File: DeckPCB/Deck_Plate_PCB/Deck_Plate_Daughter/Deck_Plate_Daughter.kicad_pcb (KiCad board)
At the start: 2 copper layers, 36 parts, among them J1 SunnyBuddy_Inhibit, J2 JST_Batt_Conn, J3 Motor_Inhibit, J4 BurnWire_Inhibit, J5 Power, J6 Raspberry_Pi_2_3, J7 Board_to_Board, Q1 Device_Q_NPN_BCE, U2 SunnyBuddy_Breakout, U3 Big_Easy_Driver, U4 TTL_Camera, U5 Adafruit_INA219_Breakout

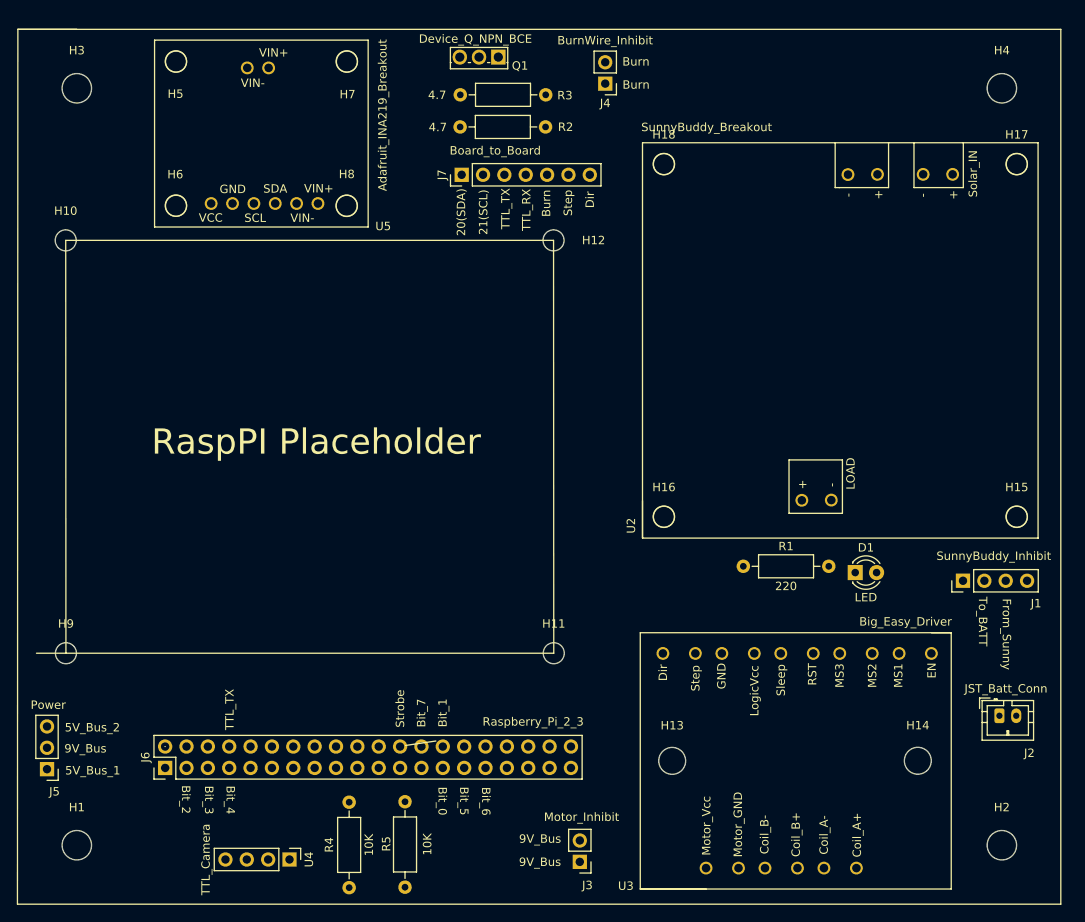
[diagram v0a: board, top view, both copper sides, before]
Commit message: Started routing of Deck_Plate_PCB, the main board.
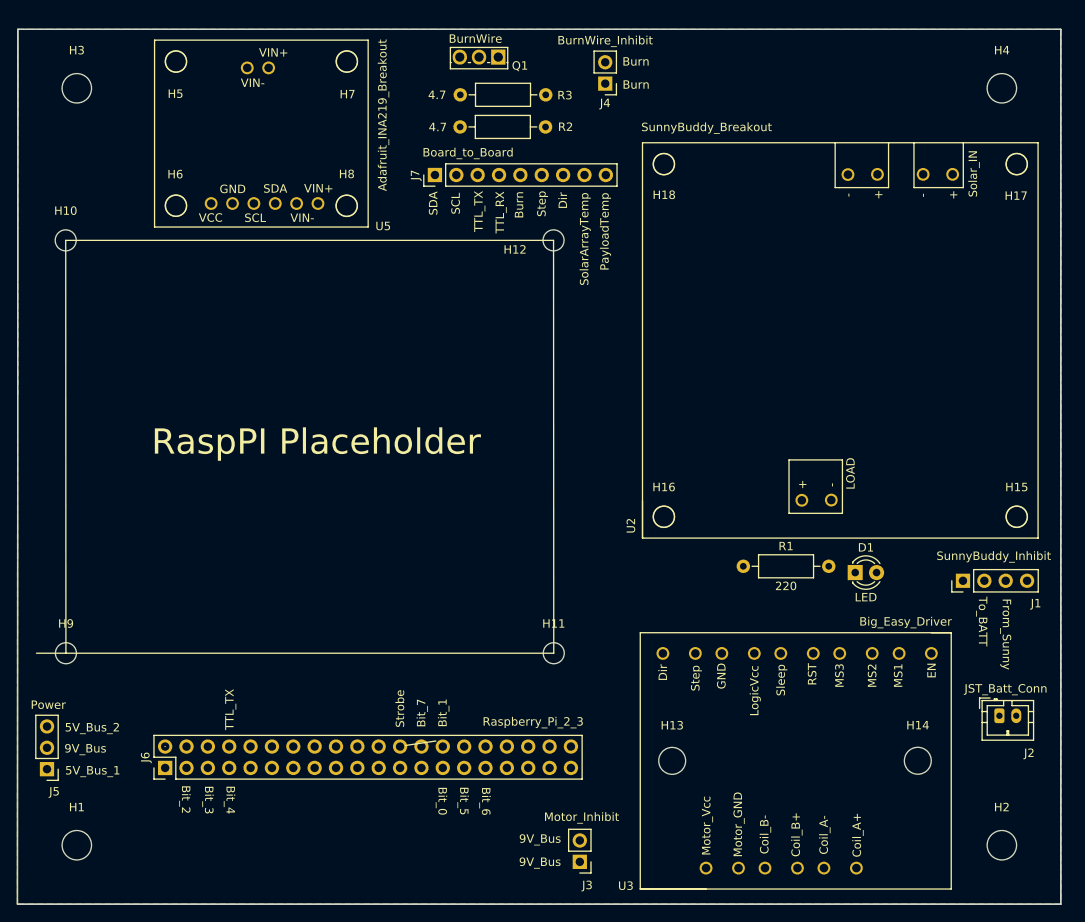
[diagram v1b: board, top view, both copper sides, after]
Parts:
- removed R4, R5: 10K, Resistor_THT:R_Axial_DIN0207_L6.3mm_D2.5mm_P10.16mm_Horizontal
- removed U4: TTL_Camera, Connector_PinHeader_2.54mm:PinHeader_1x04_P2.54mm_Vertical
- J7: footprint Connector_PinHeader_2.54mm:PinHeader_1x07_P2.54mm_Vertical -> Connector_PinHeader_2.54mm:PinHeader_1x09_P2.54mm_Vertical
- Q1: value Device_Q_NPN_BCE -> BurnWire
- moved J7 3.18 mm to (128.5, 60.8)
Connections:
- net /20(SDA) renamed /SDA
- net /21(SCL) renamed /SCL
- J6 pad 8: /TTL_TX -> Net-(J6-Pad8)
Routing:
- added copper zone on B.Cu, net GND
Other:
- board outline added: 124.1 x 104 mm
- board text added: "PayloadTemp"
- board text added: "SCL"
- board text added: "SDA"
- board text added: "SolarArrayTemp"
- board text removed: "20(SDA)"
- board text removed: "21(SCL)"

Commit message: Finised routing fro Main_Board, Daughter_Board, and BurnWire circuits. Creating SensorEndPanel board next.
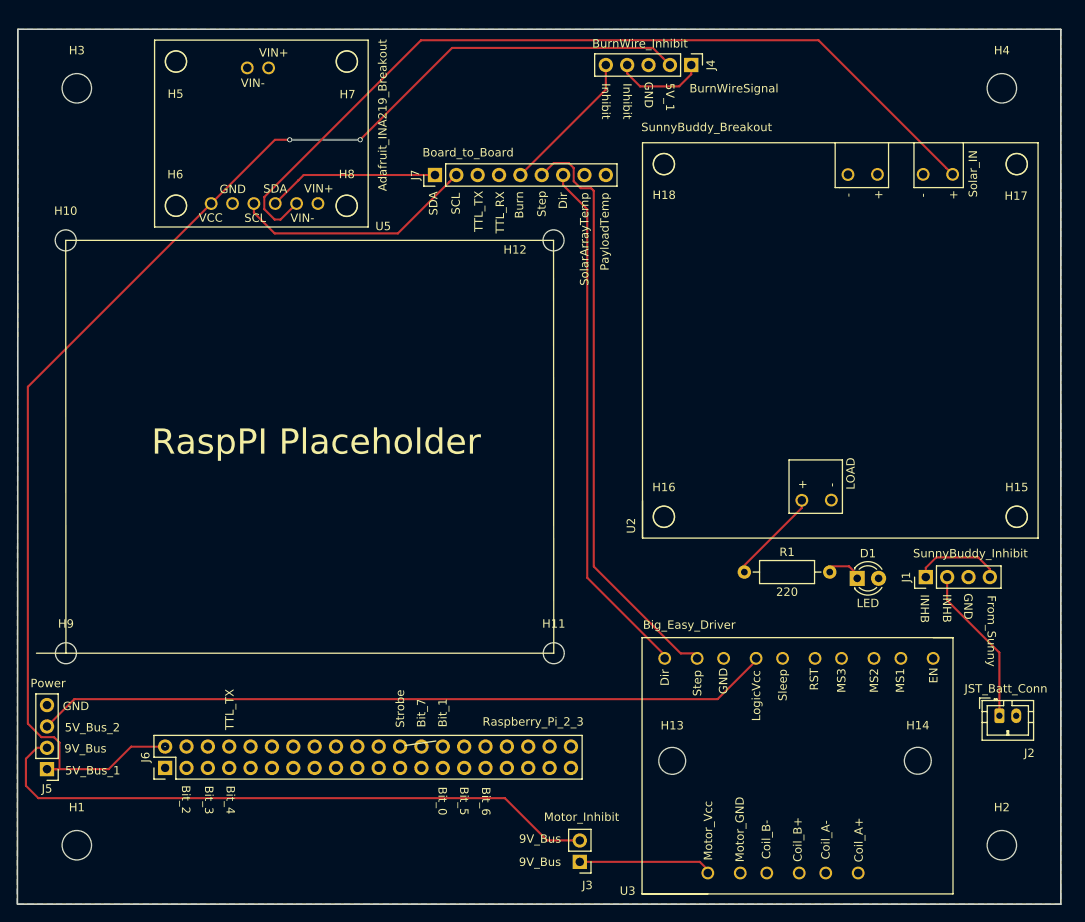
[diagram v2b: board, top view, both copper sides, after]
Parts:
- removed Q1: BurnWire, Package_TO_SOT_THT:TO-251-3_Vertical
- removed R2, R3: 4.7, Resistor_THT:R_Axial_DIN0207_L6.3mm_D2.5mm_P10.16mm_Horizontal
- J4: footprint Connector_PinHeader_2.54mm:PinHeader_1x02_P2.54mm_Vertical -> Connector_PinHeader_2.54mm:PinHeader_1x05_P2.54mm_Vertical
- J5: footprint Connector_PinHeader_2.54mm:PinHeader_1x03_P2.54mm_Vertical -> Connector_PinHeader_2.54mm:PinHeader_1x04_P2.54mm_Vertical
- moved J4 10.5 mm to (159.0, 47.8), turned to 270 degrees
- moved J1 4.45 mm to (186.9, 108.6)
- moved D1 0.73 mm to (178.7, 108.8)
- moved R1 0.70 mm to (165.3, 108.1)
- moved U3 0.62 mm to (190.1, 115.8)
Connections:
- J1 pad 1: GND -> /Sunny_Batt_Out
- J1 pad 3: /Sunny_Batt_Out -> GND
- J1 pad 4: GND -> /Sunny_Batt_Out
- J4 pad 2: /BurnWireSignal -> /5V_Bus_1
- U2 pad 1: /Solar_IN- -> GND
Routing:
- net /5V_Bus_1: track 0.00 -> 158.4 mm, vias 0 -> 2
- net /Solar_IN+: track 0.00 -> 102.8 mm
- net /9V_Bus: track 0.00 -> 90.1 mm
- net /5V_Bus_2: track 0.00 -> 88.3 mm
- net /Step: track 0.00 -> 70.1 mm
- net /Dir: track 0.00 -> 61.8 mm
- net /SCL: track 0.00 -> 29.1 mm
- net /BurnWireSignal: track 0.00 -> 28.3 mm
- net /SDA: track 0.00 -> 20.4 mm
- net /Batt_IN: track 0.00 -> 19.1 mm
- net /Sunny_Batt_Out: track 0.00 -> 10.8 mm
- net Net-(R1-Pad1): track 0.00 -> 10.7 mm
- net Net-(D1-Pad1): track 0.00 -> 3.45 mm
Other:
- board text added: "5V_1"
- board text added: "BurnWireSignal"
- board text added: "GND"
- board text added: "INHB"
- board text added: "Inhibit"
- board text removed: "To_BATT"

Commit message: updated PCB routing and creation of BurnWire circuit board and updated Daughter_Board
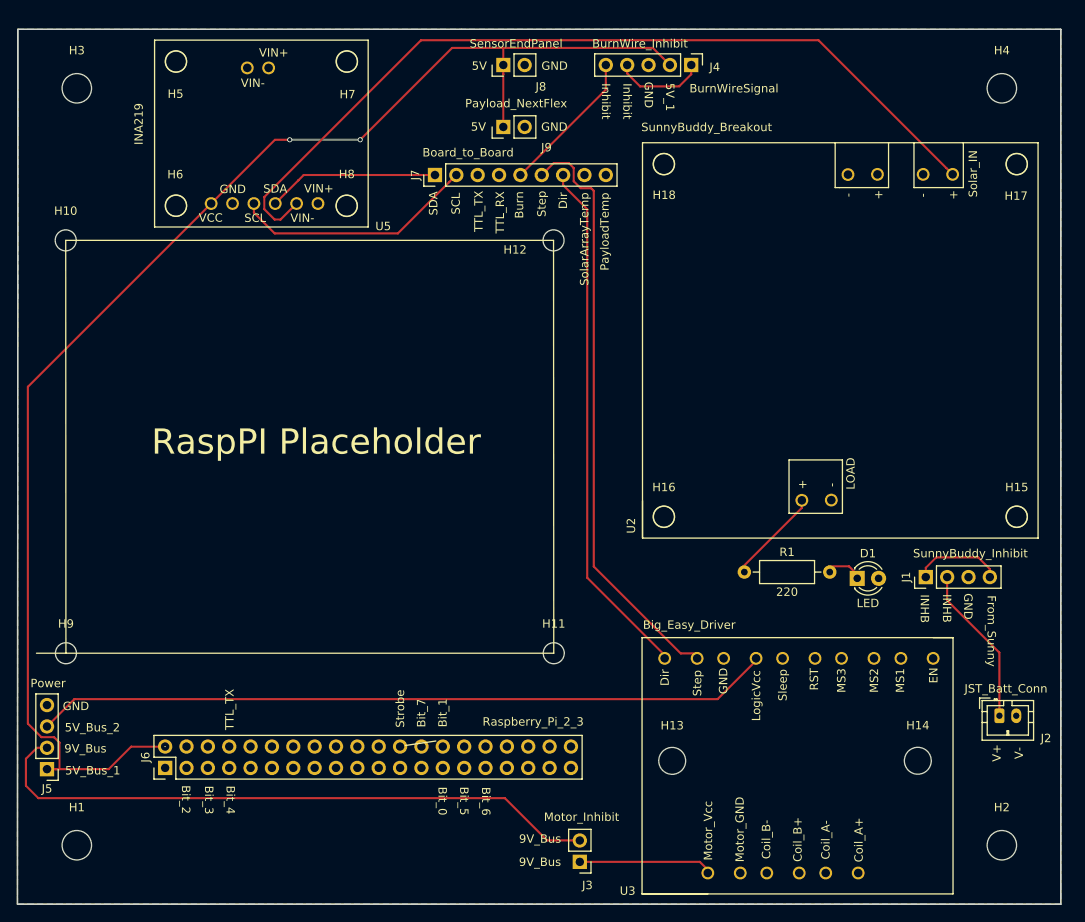
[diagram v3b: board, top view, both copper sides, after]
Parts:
- added J8: SensorEndPanel, Connector_PinHeader_2.54mm:PinHeader_1x02_P2.54mm_Vertical, F.Cu at (136.7, 47.8)
- added J9: Payload_NextFlex, Connector_PinHeader_2.54mm:PinHeader_1x02_P2.54mm_Vertical, F.Cu at (136.7, 55.1)
- U5: value Adafruit_INA219_Breakout -> INA219
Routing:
- net /5V_Bus_1: track 158.4 -> 167.8 mm
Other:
- board text added: "5V"
- board text added: "V+"
- board text added: "V-"
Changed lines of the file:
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@@
   (general
     (thickness 1.6)
-    (drawings 51)
-    (tracks 86)
+    (drawings 57)
+    (tracks 90)
     (zones 0)
-    (modules 30)
+    (modules 32)
     (nets 61)
   )
@@
     (add_net "Net-(U3-Pad6)")
   )
+  (module Connector_PinHeader_2.54mm:PinHeader_1x02_P2.54mm_Vertical (layer F.Cu)
+    (at 136.652 55.118 90)
+    (descr "Through hole straight pin header, 1x02, 2.54mm pitch, single row")
+    (tags "Through hole pin header THT 1x02 2.54mm single row")
+    (fp_text reference J9 (at -2.442 5.128 180) (layer F.SilkS)
+      (effects (font (size 1 1) (thickness 0.15)))
+    )
+    (fp_text value Payload_NextFlex (at 2.794 1.524 180) (layer F.SilkS)
+      (effects (font (size 1 1) (thickness 0.15)))
+    )
+    (fp_text user %R (at 0 1.27) (layer F.Fab)
+      (effects (font (size 1 1) (thickness 0.15)))
+    )
+    (fp_line (start 1.8 -1.8) (end -1.8 -1.8) (layer F.CrtYd) (width 0.05))
+    (fp_line (start 1.8 4.35) (end 1.8 -1.8) (layer F.CrtYd) (width 0.05))
+    (fp_line (start -1.8 4.35) (end 1.8 4.35) (layer F.CrtYd) (width 0.05))
+    (fp_line (start -1.8 -1.8) (end -1.8 4.35) (layer F.CrtYd) (width 0.05))
+    (fp_line (start -1.33 -1.33) (end 0 -1.33) (layer F.SilkS) (width 0.12))
+    (fp_line (start -1.33 0) (end -1.33 -1.33) (layer F.SilkS) (width 0.12))
+    (fp_line (start -1.33 1.27) (end 1.33 1.27) (layer F.SilkS) (width 0.12))
+    (fp_line (start 1.33 1.27) (end 1.33 3.87) (layer F.SilkS) (width 0.12))
+    (fp_line (start -1.33 1.27) (end -1.33 3.87) (layer F.SilkS) (width 0.12))
+    (fp_line (start -1.33 3.87) (end 1.33 3.87) (layer F.SilkS) (width 0.12))
+    (fp_line (start -1.27 -0.635) (end -0.635 -1.27) (layer F.Fab) (width 0.1))
+    (fp_line (start -1.27 3.81) (end -1.27 -0.635) (layer F.Fab) (width 0.1))
+    (fp_line (start 1.27 3.81) (end -1.27 3.81) (layer F.Fab) (width 0.1))
+    (fp_line (start 1.27 -1.27) (end 1.27 3.81) (layer F.Fab) (width 0.1))
+    (fp_line (start -0.635 -1.27) (end 1.27 -1.27) (layer F.Fab) (width 0.1))
+    (pad 2 thru_hole oval (at 0 2.54 90) (size 1.7 1.7) (drill 1) (layers *.Cu *.Mask)
+      (net 1 GND))
+    (pad 1 thru_hole rect (at 0 0 90) (size 1.7 1.7) (drill 1) (layers *.Cu *.Mask)
+      (net 7 /5V_Bus_1))
+    (model ${KISYS3DMOD}/Connector_PinHeader_2.54mm.3dshapes/PinHeader_1x02_P2.54mm_Vertical.wrl
+      (at (xyz 0 0 0))
+      (scale (xyz 1 1 1))
+      (rotate (xyz 0 0 0))
+    )
+  )
+  (module Connector_PinHeader_2.54mm:PinHeader_1x02_P2.54mm_Vertical (layer F.Cu)
+    (at 136.652 47.752 90)
+    (descr "Through hole straight pin header, 1x02, 2.54mm pitch, single row")
+    (tags "Through hole pin header THT 1x02 2.54mm single row")
+    (fp_text reference J8 (at -2.578 4.468 180) (layer F.SilkS)
+      (effects (font (size 1 1) (thickness 0.15)))
+    )
+    (fp_text value SensorEndPanel (at 2.54 1.524 180) (layer F.SilkS)
+      (effects (font (size 1 1) (thickness 0.15)))
+    )
+    (fp_text user %R (at 0 1.27) (layer F.Fab)
+      (effects (font (size 1 1) (thickness 0.15)))
+    )
+    (fp_line (start 1.8 -1.8) (end -1.8 -1.8) (layer F.CrtYd) (width 0.05))
+    (fp_line (start 1.8 4.35) (end 1.8 -1.8) (layer F.CrtYd) (width 0.05))
+    (fp_line (start -1.8 4.35) (end 1.8 4.35) (layer F.CrtYd) (width 0.05))
+    (fp_line (start -1.8 -1.8) (end -1.8 4.35) (layer F.CrtYd) (width 0.05))
+    (fp_line (start -1.33 -1.33) (end 0 -1.33) (layer F.SilkS) (width 0.12))
+    (fp_line (start -1.33 0) (end -1.33 -1.33) (layer F.SilkS) (width 0.12))
+    (fp_line (start -1.33 1.27) (end 1.33 1.27) (layer F.SilkS) (width 0.12))
+    (fp_line (start 1.33 1.27) (end 1.33 3.87) (layer F.SilkS) (width 0.12))
+    (fp_line (start -1.33 1.27) (end -1.33 3.87) (layer F.SilkS) (width 0.12))
+    (fp_line (start -1.33 3.87) (end 1.33 3.87) (layer F.SilkS) (width 0.12))
+    (fp_line (start -1.27 -0.635) (end -0.635 -1.27) (layer F.Fab) (width 0.1))
+    (fp_line (start -1.27 3.81) (end -1.27 -0.635) (layer F.Fab) (width 0.1))
+    (fp_line (start 1.27 3.81) (end -1.27 3.81) (layer F.Fab) (width 0.1))
+    (fp_line (start 1.27 -1.27) (end 1.27 3.81) (layer F.Fab) (width 0.1))
+    (fp_line (start -0.635 -1.27) (end 1.27 -1.27) (layer F.Fab) (width 0.1))
+    (pad 2 thru_hole oval (at 0 2.54 90) (size 1.7 1.7) (drill 1) (layers *.Cu *.Mask)
+      (net 1 GND))
+    (pad 1 thru_hole rect (at 0 0 90) (size 1.7 1.7) (drill 1) (layers *.Cu *.Mask)
+      (net 7 /5V_Bus_1))
+    (model ${KISYS3DMOD}/Connector_PinHeader_2.54mm.3dshapes/PinHeader_1x02_P2.54mm_Vertical.wrl
+      (at (xyz 0 0 0))
+      (scale (xyz 1 1 1))
+      (rotate (xyz 0 0 0))
+    )
+  )
   (module Connector_PinHeader_2.54mm:PinHeader_1x05_P2.54mm_Vertical (layer F.Cu)
     (at 159.004 47.752 270)
     (descr "Through hole straight pin header, 1x05, 2.54mm pitch, single row")
     (tags "Through hole pin header THT 1x05 2.54mm single row")
-    (fp_text reference J4 (at 0 -2.33 90) (layer F.SilkS)
+    (fp_text reference J4 (at 0.254 -2.794 180) (layer F.SilkS)
       (effects (font (size 1 1) (thickness 0.15)))
     )
@@
       (effects (font (size 1 1) (thickness 0.15)))
     )
-    (fp_text value Adafruit_INA219_Breakout (at 27.1272 8.9281 90) (layer F.SilkS)
+    (fp_text value INA219 (at -1.86888 9.9771 90) (layer F.SilkS)
       (effects (font (size 1 1) (thickness 0.15)))
     )
@@
     (descr "JST PH series connector, B2B-PH-K (http://www.jst-mfg.com/product/pdf/eng/ePH.pdf), generated with kicad-footprint-generator")
     (tags "connector JST PH side entry")
-    (fp_text reference J2 (at 3.56108 4.43992) (layer F.SilkS)
+    (fp_text reference J2 (at 5.53888 2.67928) (layer F.SilkS)
       (effects (font (size 1 1) (thickness 0.15)))
     )
@@
       (rotate (xyz 0 0 0))
     )
+  )
+  (gr_text V- (at 197.99 129.58 90) (layer F.SilkS)
+    (effects (font (size 1 1) (thickness 0.15)))
+  )
+  (gr_text V+ (at 195.34 129.57 90) (layer F.SilkS)
+    (effects (font (size 1 1) (thickness 0.15)))
+  )
+  (gr_text 5V (at 133.8 47.86) (layer F.SilkS)
+    (effects (font (size 1 1) (thickness 0.15)))
+  )
+  (gr_text GND (at 142.75 47.86) (layer F.SilkS)
+    (effects (font (size 1 1) (thickness 0.15)))
+  )
+  (gr_text GND (at 142.72 55.11) (layer F.SilkS)
+    (effects (font (size 1 1) (thickness 0.15)))
+  )
+  (gr_text 5V (at 133.7 55.1) (layer F.SilkS)
+    (effects (font (size 1 1) (thickness 0.15)))
   )
   (gr_text BurnWireSignal (at 164.084 50.546) (layer F.SilkS)
@@
   (segment (start 119.634 56.642) (end 130.556 45.72) (width 0.25) (layer F.Cu) (net 7))
   (segment (start 154.432 45.72) (end 155.614001 46.902001) (width 0.25) (layer F.Cu) (net 7))
-  (segment (start 130.556 45.72) (end 154.432 45.72) (width 0.25) (layer F.Cu) (net 7))
+  (segment (start 136.652 47.752) (end 136.652 45.72) (width 0.25) (layer F.Cu) (net 7))
+  (segment (start 130.556 45.72) (end 136.652 45.72) (width 0.25) (layer F.Cu) (net 7))
+  (segment (start 136.652 45.72) (end 154.432 45.72) (width 0.25) (layer F.Cu) (net 7))
+  (segment (start 136.652 48.852) (end 136.652 55.118) (width 0.25) (layer F.Cu) (net 7))
+  (segment (start 136.652 47.752) (end 136.652 48.852) (width 0.25) (layer F.Cu) (net 7))
   (segment (start 166.50208 118.79072) (end 166.50208 117.729) (width 0.25) (layer F.Cu) (net 8))
   (segment (start 162.1282 123.1646) (end 166.50208 118.79072) (width 0.25) (layer F.Cu) (net 8))
@@
     (polygon
       (pts
-        (xy 202.946 147.5486) (xy 78.8416 147.5486) (xy 78.9178 43.5102) (xy 202.9714 43.5102)
+        (xy 202.95 147.55) (xy 78.875 147.55) (xy 78.925 43.5) (xy 202.95 43.5)
       )
     )

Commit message: Updated PCB for NASA analog lines and signal conditioning circuitry. Added Gerber file ZIP for DECK_PLATE_MAIN
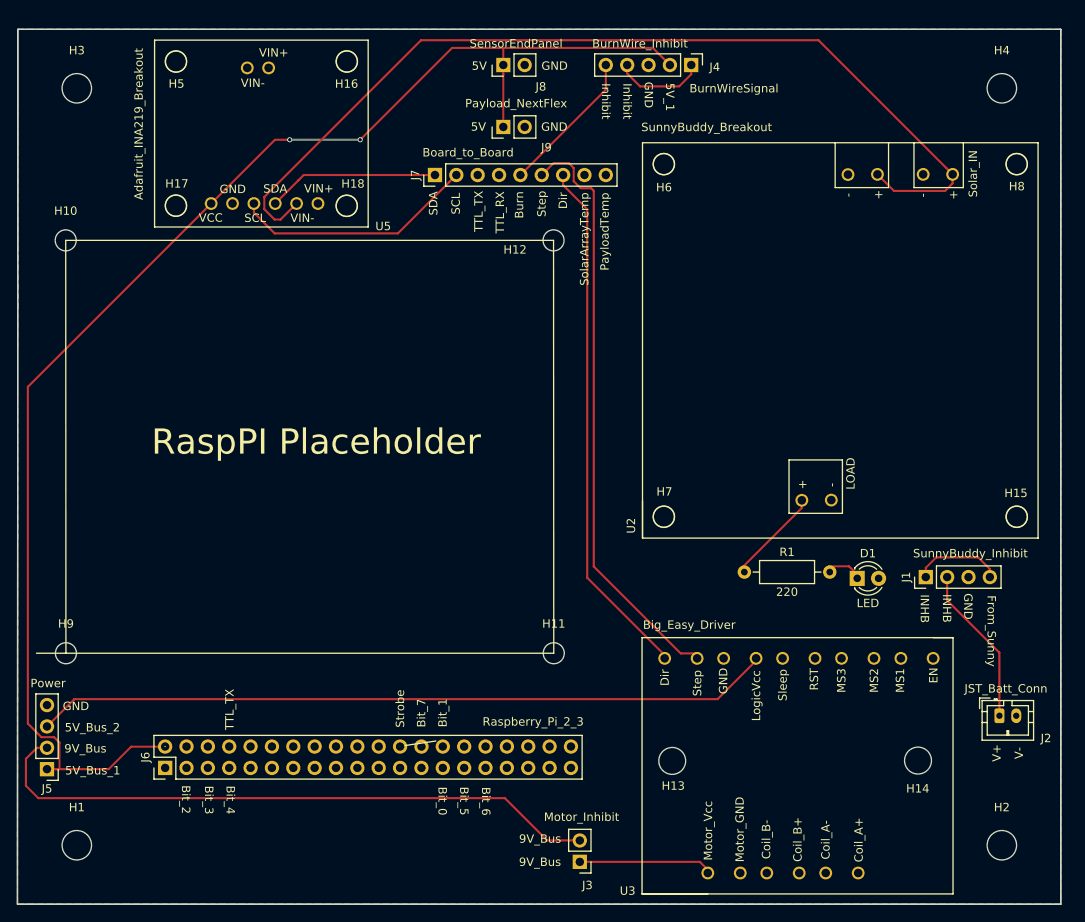
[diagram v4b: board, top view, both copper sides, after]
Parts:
- H13, H14: footprint MountingHole:MountingHole_3.2mm_M3 -> Deck_Plate_PCB:BigEasy_MountingHole_3.2mm_M3
- H15, H5: footprint MountingHole:MountingHole_2.5mm -> Deck_Plate_PCB:Accel_MountingHole_2.5mm
- H16, H17, H18: value SunnyMount -> INA219; footprint MountingHole:MountingHole_2.5mm -> Deck_Plate_PCB:Accel_MountingHole_2.5mm
- H6, H7, H8: value INA219 -> SunnyMount; footprint MountingHole:MountingHole_2.5mm -> Deck_Plate_PCB:Accel_MountingHole_2.5mm
- U5: value INA219 -> Adafruit_INA219_Breakout
- moved H17 100.1 mm to (97.7, 64.5)
- moved H8 79.8 mm to (197.7, 59.5)
- moved H16 66.0 mm to (118.0, 47.3)
- moved H7 66.0 mm to (155.7, 101.5)
- moved H6 58.2 mm to (155.7, 59.5)
- moved H18 38.0 mm to (118.0, 64.5)
- moved H14 0.08 mm to (186.0, 130.5)
- moved H13 0.05 mm to (156.8, 130.5)
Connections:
- net Net-(J6-Pad10) renamed /Bit_14
- net Net-(J6-Pad11) renamed /Bit_16
- net Net-(J6-Pad19) renamed /Bit_9
- net Net-(J6-Pad21) renamed /Bit_8
- net Net-(J6-Pad23) renamed /Bit_10
- net Net-(J6-Pad32) renamed /Bit_11
- net Net-(J6-Pad33) renamed /Bit_12
- net Net-(J6-Pad36) renamed /Bit_15
- net Net-(J6-Pad8) renamed /Bit_13
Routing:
- net /Solar_IN+: track 102.8 -> 114.0 mm
